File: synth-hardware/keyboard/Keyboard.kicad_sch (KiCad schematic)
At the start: 62 parts, among them K1 SELECT, K10 F#1, K11 G1, K12 G#1, K13 A1, K14 A#1, K15 B1, K16 C2, K17 C#2, K18 D2, K19 D#2, K2 UP, K20 E2, K21 F2, K22 F#2, K23 G2, K24 G#2, K25 A2, K26 A#2, K27 B2, K28 SELECT, K29 SELECT, K3 DOWN, K30 SELECT, K31 SELECT, K32 SELECT, K4 C1, K5 C#1, K6 D1, K7 D#1, K8 E1, K9 F1, U1 RP2040

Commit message: feat(hardware): first revision pcb
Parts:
- removed K28, K29, K30, K31, K32: SELECT, KeyboardFootprints:Generic_MX_PCB_1u, symbol KeyboardSymbols:GenericSwitch
- removed ST1: C_STAB, PCM_marbastlib-mx:STAB_MX_2u, symbol PCM_marbastlib-mx:MX_stab
- removed ST2: D_STAB, PCM_marbastlib-mx:STAB_MX_2u, symbol PCM_marbastlib-mx:MX_stab
- removed ST3: E_STAB, PCM_marbastlib-mx:STAB_MX_2u, symbol PCM_marbastlib-mx:MX_stab
- removed ST4: F_STAB, PCM_marbastlib-mx:STAB_MX_2u, symbol PCM_marbastlib-mx:MX_stab
- removed ST5: G_STAB, PCM_marbastlib-mx:STAB_MX_2u, symbol PCM_marbastlib-mx:MX_stab
- removed ST6: A_STAB, PCM_marbastlib-mx:STAB_MX_2u, symbol PCM_marbastlib-mx:MX_stab
- removed ST7: B_STAB, PCM_marbastlib-mx:STAB_MX_2u, symbol PCM_marbastlib-mx:MX_stab
- added AM2: CD74HC4067SM, Package_SO:SSOP-24_5.3x8.2mm_P0.65mm, symbol 74xx:CD74HC4067SM
- added C1, C12, C2, C4, C6: 1uF, Capacitor_SMD:C_0402_1005Metric, symbol Device:C_Small
- added C10, C11: 22pF, Capacitor_SMD:C_0402_1005Metric, symbol Device:C_Small
- added C13, C14, C15, C16, C5, C7, C8, C9: 100nF, Capacitor_SMD:C_0402_1005Metric, symbol Device:C_Small
- added C3: 10uF, Capacitor_SMD:C_0603_1608Metric, symbol Device:C_Small
- added D1: Power LED (Green), LED_SMD:LED_0805_2012Metric, symbol Device:LED_Small
- added F1: Fuse_Small, Fuse:Fuse_1206_3216Metric, symbol Device:Fuse_Small
- added FID1, FID2, FID3: Fiducial, Fiducial:Fiducial_1mm_Mask2mm, symbol Mechanical:Fiducial
- added J1: USB_C_Receptacle_USB2.0_16P, Connector_USB:USB_C_Receptacle_HRO_TYPE-C-31-M-12, symbol Connector:USB_C_Receptacle_USB2.0_16P
- added J2: Conn_01x04, Connector_JST:JST_SH_SM04B-SRSS-TB_1x04-1MP_P1.00mm_Horizontal, symbol Connector_Generic:Conn_01x04
- added J3: Conn_01x05, Connector_PinHeader_2.54mm:PinHeader_1x05_P2.54mm_Vertical, symbol Connector_Generic:Conn_01x05
- added R1, R2, R3, R8, R9: 5.1k ohm, Resistor_SMD:R_0402_1005Metric, symbol Device:R_Small
- added R10, R6, R7: 1k ohm, Resistor_SMD:R_0402_1005Metric, symbol Device:R_Small
- added R4, R5: 27 ohm, Resistor_SMD:R_0201_0603Metric, symbol Device:R_Small
- added S16: C, Package_TO_SOT_SMD:SOT-23, symbol KeyboardSymbols:3PinHallEffect
- added S17: C#, Package_TO_SOT_SMD:SOT-23, symbol KeyboardSymbols:3PinHallEffect
- added S18: D, Package_TO_SOT_SMD:SOT-23, symbol KeyboardSymbols:3PinHallEffect
- added S19: D#, Package_TO_SOT_SMD:SOT-23, symbol KeyboardSymbols:3PinHallEffect
- added S20: E, Package_TO_SOT_SMD:SOT-23, symbol KeyboardSymbols:3PinHallEffect
- added S21: F, Package_TO_SOT_SMD:SOT-23, symbol KeyboardSymbols:3PinHallEffect
- added S22: F#, Package_TO_SOT_SMD:SOT-23, symbol KeyboardSymbols:3PinHallEffect
- added S23: G, Package_TO_SOT_SMD:SOT-23, symbol KeyboardSymbols:3PinHallEffect
- added S24: G#, Package_TO_SOT_SMD:SOT-23, symbol KeyboardSymbols:3PinHallEffect
- added S25: A, Package_TO_SOT_SMD:SOT-23, symbol KeyboardSymbols:3PinHallEffect
- added S26: A#, Package_TO_SOT_SMD:SOT-23, symbol KeyboardSymbols:3PinHallEffect
- added S27: B, Package_TO_SOT_SMD:SOT-23, symbol KeyboardSymbols:3PinHallEffect
- added SW1: RESET, Button_Switch_SMD:SW_SPST_TL3342, symbol Switch:SW_Push
- added SW2: BOOTSELECT, Button_Switch_SMD:SW_SPST_TL3342, symbol Switch:SW_Push
- added U2: XC6206PxxxMR, Package_TO_SOT_SMD:SOT-23-3, symbol Regulator_Linear:XC6206PxxxMR
- added U3: SRV05-4, PCM_marbastlib-various:SOT-23-6-routable, symbol PCM_marbastlib-various:SRV05-4
- added U4: W25Q128JVS, Package_SO:SOIC-8_5.23x5.23mm_P1.27mm, symbol Memory_Flash:W25Q128JVS
- added Y1: 12MHz 20pF, Crystal:Crystal_SMD_3225-4Pin_3.2x2.5mm, symbol Device:Crystal_GND24
- AM1: LCSC (none) -> C98457
- H1, H2, H3, H4, H5, H6, K10, K11, K12, K13, K14, K15, K16, K17, K18, K19, K2, K20, K21, K22, K23, K24, K25, K26, K27, K3, K4, K5, K6, K7, K8, K9: now left out of the parts list
- K1: value SELECT -> SHIFT; now left out of the parts list
- S1, S10, S11, S12, S13, S14, S15, S2, S3, S4, S5, S6, S7, S8, S9: LCSC (none) -> C266230; MPN (none) -> GH39FKSW; Notes (none) -> Alternate part: OH49E-S (C85573)
- U1: LCSC (none) -> C2040
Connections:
- net +3.3V is gone; now on net +3V3: AM1.24 (VCC), S1.1 (VDD), S10.1 (VDD), S11.1 (VDD), S12.1 (VDD), S13.1 (VDD), S14.1 (VDD), S15.1 (VDD), S2.1 (VDD), S3.1 (VDD), S4.1 (VDD), S5.1 (VDD), S6.1 (VDD), S7.1 (VDD), S8.1 (VDD), S9.1 (VDD)
- net AM0 is gone; now on net AM1_COM: AM1.1 (COM)
- net GND: now also AM1.6 (I3), U1.19 (TESTEN), U1.57 (GND), AM2.12 (GND), AM2.15 (~{E}), AM2.18 (I13), AM2.19 (I12), AM2.20 (I11), AM2.6 (I3), C1.2, C10.1, C11.1, C12.2, C13.2, C14.2, C15.2, C16.2, C2.2, C3.2, C4.2, C5.2, C6.2, C7.2, C8.2, C9.2, J1.A1 (GND), J1.A12 (GND), J1.B1 (GND), J1.B12 (GND), J1.S1 (SHIELD), J2.4 (Pin_4), J3.5 (Pin_5), R1.2, R2.2, S16.3 (GND), S17.3 (GND), S18.3 (GND), S19.3 (GND), S20.3 (GND), S21.3 (GND), S22.3 (GND), S23.3 (GND), S24.3 (GND), S25.3 (GND), S26.3 (GND), S27.3 (GND), SW1.1, SW2.1, U2.1 (GND), U3.2 (VN), U4.4 (GND), Y1.2, Y1.4
- net SELECT0: now also U1.6 (GPIO4)
- net SELECT1: now also U1.5 (GPIO3)
- net SELECT2: now also U1.3 (GPIO1)
- net SELECT3: now also U1.4 (GPIO2)
- net +3V3: now reaches U1.1 (IOVDD), U1.10 (IOVDD), U1.22 (IOVDD), U1.33 (IOVDD), U1.42 (IOVDD), U1.49 (IOVDD)
- net +3V3: now also U1.43 (ADC_AVDD), U1.44 (VREG_IN), U1.48 (USB_VDD), AM2.24 (VCC), C12.1, C14.1, C15.1, C16.1, C2.1, C3.1, C6.1, C7.1, C8.1, C9.1, J3.4 (Pin_4), R10.1, R3.2, R9.2, S16.1 (VDD), S17.1 (VDD), S18.1 (VDD), S19.1 (VDD), S20.1 (VDD), S21.1 (VDD), S22.1 (VDD), S23.1 (VDD), S24.1 (VDD), S25.1 (VDD), S26.1 (VDD), S27.1 (VDD), U2.2 (VO), U4.8 (VCC)
- net USER_LED: now reaches U1.2 (GPIO0)
- net USER_LED: now also D1.1 (K)
- net XIN: now reaches U1.20 (XIN)
- net XIN: now also C10.2, Y1.3
- net XOUT: now reaches U1.21 (XOUT)
- net XOUT: now also R6.2
- net +1V1: now reaches U1.23 (DVDD), U1.50 (DVDD)
- net +1V1: now also U1.45 (VREG_VOUT), C13.1, C4.1, C5.1
- net SWC: now reaches U1.24 (SWCLK)
- net SWC: now also J3.3 (Pin_3)
- net SWD: now reaches U1.25 (SWD)
- net SWD: now also J3.2 (Pin_2)
- net RESET: now reaches U1.26 (RUN)
- net RESET: now also J3.1 (Pin_1), R3.1, SW1.2
- net SELECT6: now reaches U1.34 (GPIO22)
- net SELECT6: now also AM2.14 (S2)
- net SELECT7: now reaches U1.35 (GPIO23)
- net SELECT7: now also AM2.13 (S3)
- net SELECT5: now reaches U1.36 (GPIO24)
- net SELECT5: now also AM2.11 (S1)
- net SELECT4: now reaches U1.37 (GPIO25)
- net SELECT4: now also AM2.10 (S0)
- net AM1_COM: now reaches U1.38 (GPIO26_ADC0)
- net AM2_COM: now reaches U1.39 (GPIO27_ADC1)
- net AM2_COM: now also AM2.1 (COM)
- net at U1.46 (USB_DM): now also R5.2
- net at U1.47 (USB_DP): now also R4.2
- net Q_IO3: now reaches U1.51 (QSPI_SD3)
- net Q_IO3: now also U4.7 (IO3)
- net Q_CLK: now reaches U1.52 (QSPI_SCLK)
- net Q_CLK: now also U4.6 (CLK)
- net Q_IO0: now reaches U1.53 (QSPI_SD0)
- net Q_IO0: now also U4.5 (DI(IO0))
- net Q_IO2: now reaches U1.54 (QSPI_SD2)
- net Q_IO2: now also U4.3 (IO2)
- net Q_IO1: now reaches U1.55 (QSPI_SD1)
- net Q_IO1: now also U4.2 (DO(IO1))
- net Q_SEL: now reaches U1.56 (QSPI_SS)
- net Q_SEL: now also R7.2, R8.1, U4.1 (~{CS})
- net AM0:0 renamed AM1:0
- net AM1:0: now also S14.2 (OUT); no longer S6.2 (OUT)
- net AM0:1 renamed AM1:1
- net AM1:1: now also S12.2 (OUT); no longer S4.2 (OUT)
- net AM0:10 renamed AM1:10
- net AM1:10: now also S6.2 (OUT); no longer S10.2 (OUT)
- net AM0:11 renamed AM1:11
- net AM1:11: now also S8.2 (OUT); no longer S15.2 (OUT)
- net AM0:12 renamed AM1:12
- net AM1:12: now also S9.2 (OUT); no longer S13.2 (OUT)
- net AM0:13 renamed AM1:13
- net AM0:14 renamed AM1:14
- net AM1:14: now also S13.2 (OUT); no longer S9.2 (OUT)
- net AM0:15 renamed AM1:15
- net AM1:15: now also S15.2 (OUT); no longer S8.2 (OUT)
- net AM0:2 renamed AM1:2
- net AM1:2: now also S10.2 (OUT); no longer S3.2 (OUT)
- net AM0:3 renamed AM1:7
- net AM1:7: now also AM1.2 (I7); no longer AM1.6 (I3)
- net AM0:4 renamed AM1:4
- net AM1:4: now also S7.2 (OUT)
- net AM0:5 renamed AM1:5
- net AM1:5: now also S5.2 (OUT); no longer S7.2 (OUT)
- net AM0:6 renamed AM1:6
- net AM1:6: now also S1.2 (OUT); no longer S5.2 (OUT)
- removed net AM0:7: AM1.2 (I7), S1.2 (OUT)
- net AM0:8 renamed AM1:8
- net AM1:8: now also S3.2 (OUT); no longer S14.2 (OUT)
- net AM0:9 renamed AM1:9
- net AM1:9: now also S4.2 (OUT); no longer S12.2 (OUT)
- new net: R7.1, SW2.2
- new net: J1.A5 (CC1), R1.1
- new net: J1.B5 (CC2), R2.1
- new net: C11.2, R6.1, Y1.1
- new net: D1.2 (A), R10.2
- new net: R8.2, R9.1
- new net +5V: C1.1, F1.2, J2.1 (Pin_1), U2.3 (VI), U3.5 (VP)
- new net AM2:0: AM2.9 (I0), S16.2 (OUT)
- new net AM2:1: AM2.8 (I1), S18.2 (OUT)
- new net AM2:10: AM2.21 (I10), S22.2 (OUT)
- new net AM2:14: AM2.17 (I14), S19.2 (OUT)
- new net AM2:15: AM2.16 (I15), S17.2 (OUT)
- new net AM2:2: AM2.7 (I2), S20.2 (OUT)
- new net AM2:4: AM2.5 (I4), S21.2 (OUT)
- new net AM2:5: AM2.4 (I5), S23.2 (OUT)
- new net AM2:6: AM2.3 (I6), S25.2 (OUT)
- new net AM2:7: AM2.2 (I7), S27.2 (OUT)
- new net AM2:8: AM2.23 (I8), S26.2 (OUT)
- new net AM2:9: AM2.22 (I9), S24.2 (OUT)
- new net D+: J1.A6 (D+), J1.B6 (D+), J2.3 (Pin_3), R4.1, U3.1 (IO1)
- new net D-: J1.A7 (D-), J1.B7 (D-), J2.2 (Pin_2), R5.1, U3.6 (IO4)
- new net VBUS: F1.1, J1.A4 (VBUS), J1.A9 (VBUS), J1.B4 (VBUS), J1.B9 (VBUS)
- no-connect marks 0 -> 23
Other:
- note added: "Analog Multiplexers"
- note added: "Crystal Oscillator"
- note added: "Decoupling Capacitors"
- note added: "ESD Protection"
- note added: "Fiducials"
- note added: "IC"
- note added: "JST Connector (for USB daughter board)"
- note added: "Key Switches"
- note added: "Linear Hall Effect Sensors"
- note added: "Microcontroller"
- note added: "Mounting Holes"
- note added: "QSPI Flash"
- note added: "Reset Switch"
- note added: "Select Switch"
- note added: "USB-C Connector"
- note added: "User LED"
- note added: "Voltage Regulator"
- title: (none) -> Analog MIDI Keyboard
- moved on the sheet: AM1, H1, H2, H3, H4, H5, H6, K1, K10, K11, K12, K13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

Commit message: feat(hardware): fix usb and add more components
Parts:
- removed R3: 5.1k ohm, Resistor_SMD:R_0402_1005Metric, symbol Device:R_Small
- removed SW1: RESET, Button_Switch_SMD:SW_SPST_TL3342, symbol Switch:SW_Push
- C10, C11: LCSC C1557 -> C1555
- F1, U2: LCSC (none) -> ??
- J1: LCSC (none) -> C165948
- R4, R5: footprint Resistor_SMD:R_0201_0603Metric -> Resistor_SMD:R_0603_1608Metric
- S1, S10, S11, S12, S13, S14, S15, S16, S17, S18, S19, S2, S20, S21, S22, S23, S24, S25, S26, S27, S3, S4, S5, S6, S7, S8, S9: footprint Package_TO_SOT_SMD:SOT-23 -> Package_TO_SOT_SMD:SOT-23-3
- U3: LCSC (none) -> C558418
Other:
- note added: "<EMPTY>"
- note added: "Bootselect Switch"
- note removed: "Reset Switch"
- note removed: "Select Switch"
- moved on the sheet: C12, C13, C4, C5, C9, D1, K1, K10, K11, K12, K13, K14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

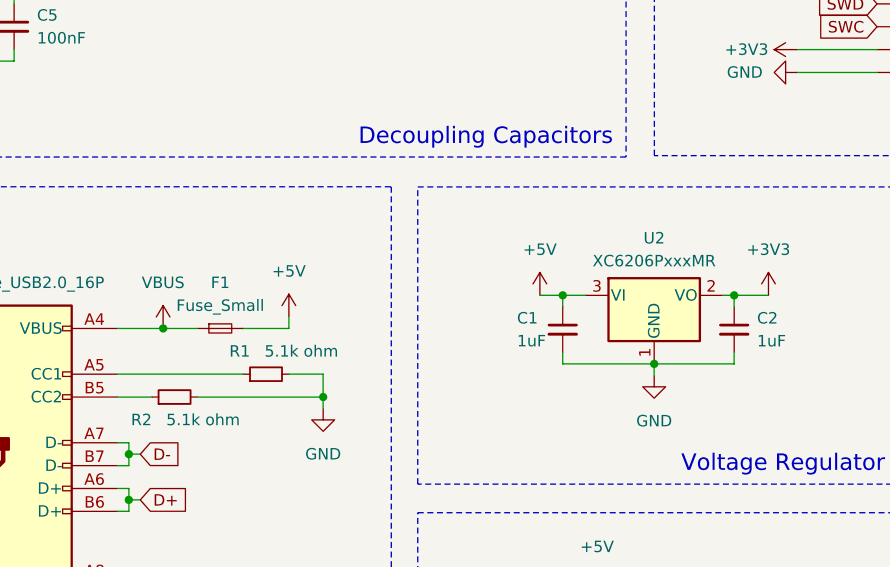
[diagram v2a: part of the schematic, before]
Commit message: feat(hardware): finished adding lcsc for all components
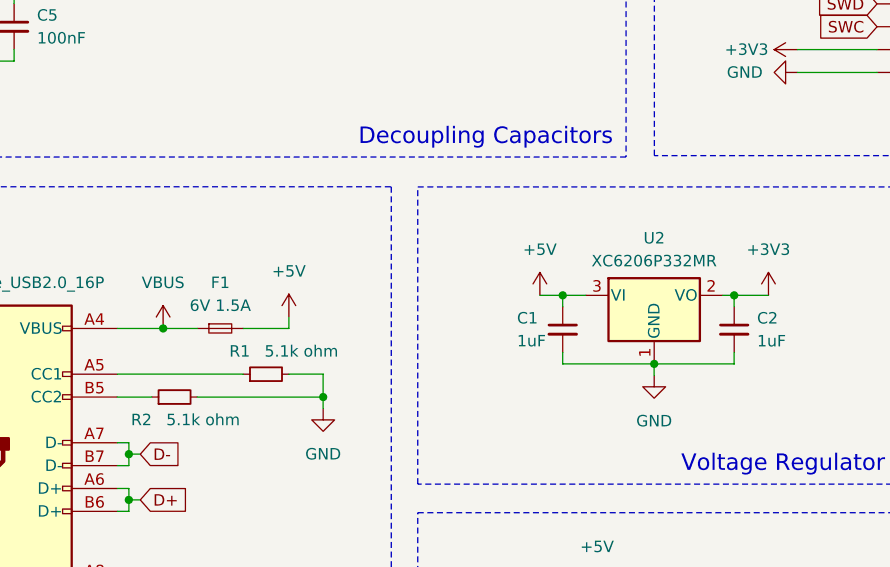
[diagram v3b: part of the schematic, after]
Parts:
- F1: value Fuse_Small -> 6V 1.5A; LCSC ?? -> C2838983
- U2: value XC6206PxxxMR -> XC6206P332MR; footprint Package_TO_SOT_SMD:SOT-23-3 -> Package_TO_SOT_SMD:SOT-23; LCSC ?? -> C5148692
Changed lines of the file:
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@@
 			)
 		)
-		(property "Value" "Fuse_Small"
+		(property "Value" "6V 1.5A"
 			(at 182.9306 227.2001 0)
 			(effects
@@
 			)
 		)
-		(property "LCSC" "??"
+		(property "LCSC" "C2838983"
 			(at 182.9306 229.7401 0)
 			(effects
@@
 			)
 		)
-		(property "Value" "XC6206PxxxMR"
+		(property "Value" "XC6206P332MR"
 			(at 231.14 222.25 0)
 			(effects
@@
 			)
 		)
-		(property "Footprint" "Package_TO_SOT_SMD:SOT-23-3"
+		(property "Footprint" "Package_TO_SOT_SMD:SOT-23"
 			(at 231.14 220.345 0)
 			(effects
@@
 			)
 		)
-		(property "LCSC" "??"
+		(property "LCSC" "C5148692"
 			(at 231.14 226.06 0)
 			(effects

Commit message: feat: dump of hardware changes and firmware
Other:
- note added: "Debug Header"
- company: (none) -> Paul Lavender-Jones
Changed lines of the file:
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@@
 		(title "Analog MIDI Keyboard")
 		(date "2024-10-21")
+		(rev "A")
+		(company "Paul Lavender-Jones")
 	)
 	(junction
@@
 		)
 	)
-	(text "ESD Protection"
+	(text "Debug Header"
 		(exclude_from_sim no)
 		(at 282.956 208.788 0)
